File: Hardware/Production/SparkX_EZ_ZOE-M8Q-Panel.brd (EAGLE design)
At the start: 187.2 x 136.7 mm, 1506 parts, among them J1 U.FL, J10 U.FL, J11 U.FL, J12 U.FL, J13 U.FL, J14 U.FL, J15 U.FL, J16 U.FL, J17 U.FL, J18 U.FL, J19 U.FL, J2 U.FL, J20 U.FL, J21 U.FL, J22 U.FL, J23 U.FL, J24 U.FL, J25 U.FL, J26 U.FL, J27 U.FL, J28 U.FL, J29 U.FL, J3 U.FL, J30 U.FL, J4 U.FL, J5 U.FL, J6 U.FL, J7 U.FL, J8 U.FL, J9 U.FL, Q1 20V/4.2A/52mΩ/1.4W, Q10 20V/4.2A/52mΩ/1.4W, Q11 20V/4.2A/52mΩ/1.4W, Q12 20V/4.2A/52mΩ/1.4W, Q13 20V/4.2A/52mΩ/1.4W, Q14 20V/4.2A/52mΩ/1.4W, Q15 20V/4.2A/52mΩ/1.4W, Q16 20V/4.2A/52mΩ/1.4W, Q17 20V/4.2A/52mΩ/1.4W, Q18 20V/4.2A/52mΩ/1.4W, Q19 20V/4.2A/52mΩ/1.4W, Q2 20V/4.2A/52mΩ/1.4W, Q20 20V/4.2A/52mΩ/1.4W, Q21 20V/4.2A/52mΩ/1.4W, Q22 20V/4.2A/52mΩ/1.4W, Q23 20V/4.2A/52mΩ/1.4W, Q24 20V/4.2A/52mΩ/1.4W, Q25 20V/4.2A/52mΩ/1.4W, Q26 20V/4.2A/52mΩ/1.4W, Q27 20V/4.2A/52mΩ/1.4W, Q28 20V/4.2A/52mΩ/1.4W, Q29 20V/4.2A/52mΩ/1.4W, Q3 20V/4.2A/52mΩ/1.4W, Q30 20V/4.2A/52mΩ/1.4W, Q4 20V/4.2A/52mΩ/1.4W, Q5 20V/4.2A/52mΩ/1.4W, Q6 20V/4.2A/52mΩ/1.4W, Q7 20V/4.2A/52mΩ/1.4W, Q8 20V/4.2A/52mΩ/1.4W, Q9 20V/4.2A/52mΩ/1.4W, U1 U-BLOX_ZOE_M8Q-0-10, U10 U-BLOX_ZOE_M8Q-0-10, U11 U-BLOX_ZOE_M8Q-0-10, U12 U-BLOX_ZOE_M8Q-0-10, U13 U-BLOX_ZOE_M8Q-0-10, U14 U-BLOX_ZOE_M8Q-0-10, U15 U-BLOX_ZOE_M8Q-0-10, U16 U-BLOX_ZOE_M8Q-0-10, U17 U-BLOX_ZOE_M8Q-0-10, U18 U-BLOX_ZOE_M8Q-0-10, U19 U-BLOX_ZOE_M8Q-0-10, U2 U-BLOX_ZOE_M8Q-0-10, U20 U-BLOX_ZOE_M8Q-0-10, U21 U-BLOX_ZOE_M8Q-0-10, U22 U-BLOX_ZOE_M8Q-0-10, U23 U-BLOX_ZOE_M8Q-0-10, U24 U-BLOX_ZOE_M8Q-0-10, U25 U-BLOX_ZOE_M8Q-0-10, U26 U-BLOX_ZOE_M8Q-0-10, U27 U-BLOX_ZOE_M8Q-0-10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

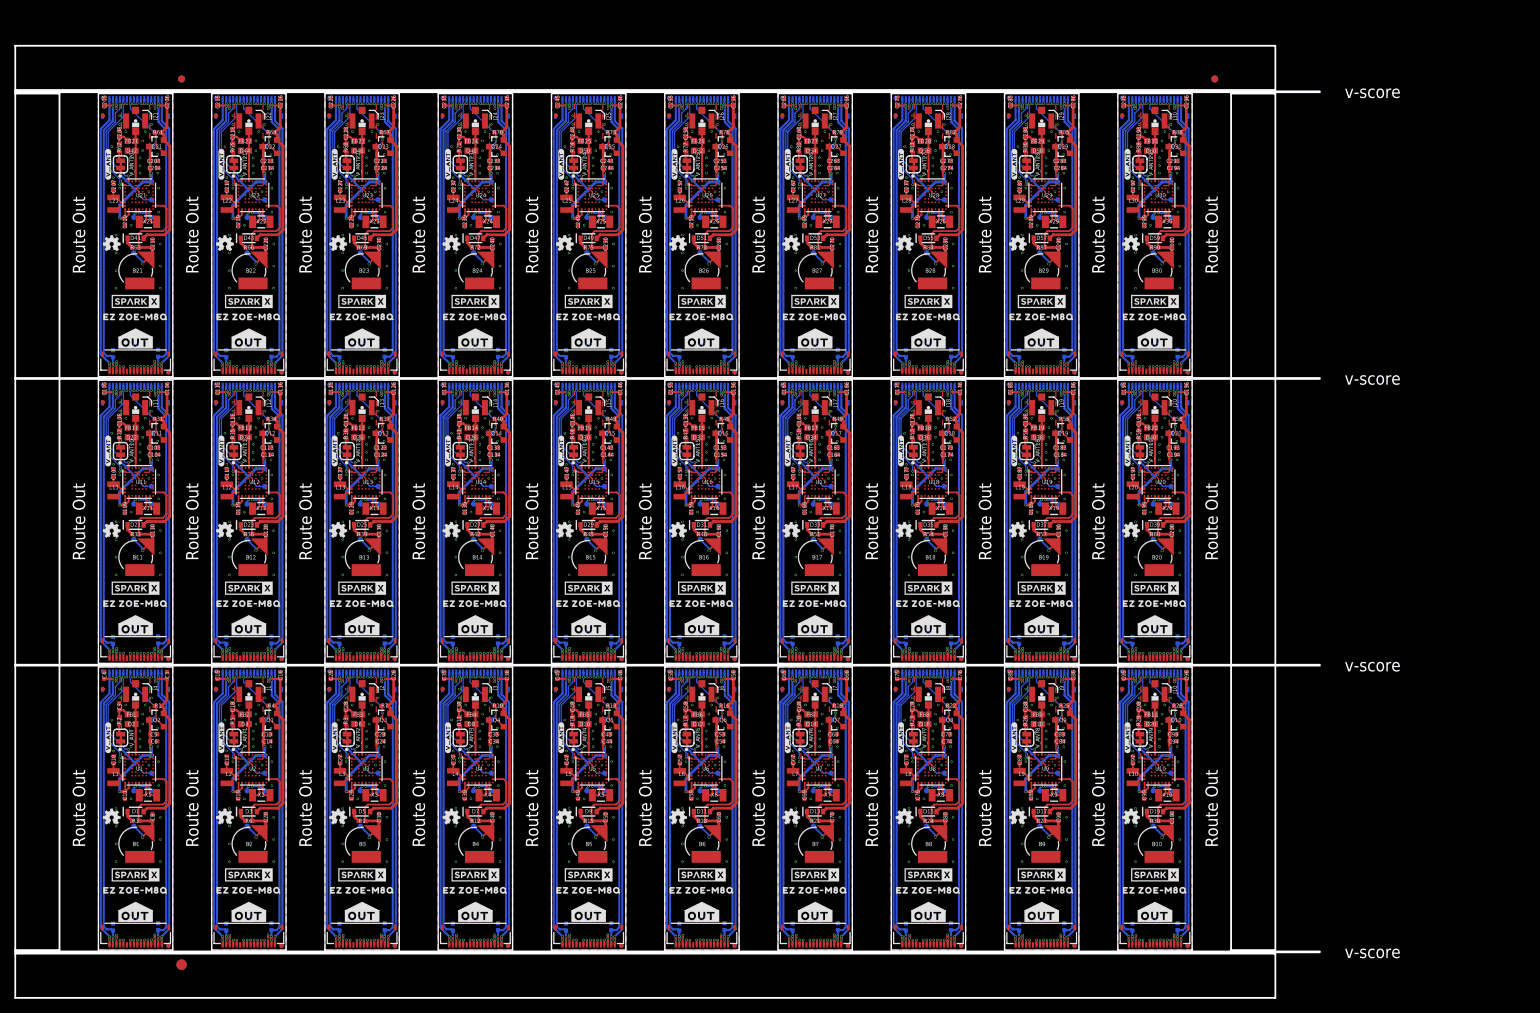
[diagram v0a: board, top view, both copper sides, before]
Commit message: Gapless production panel
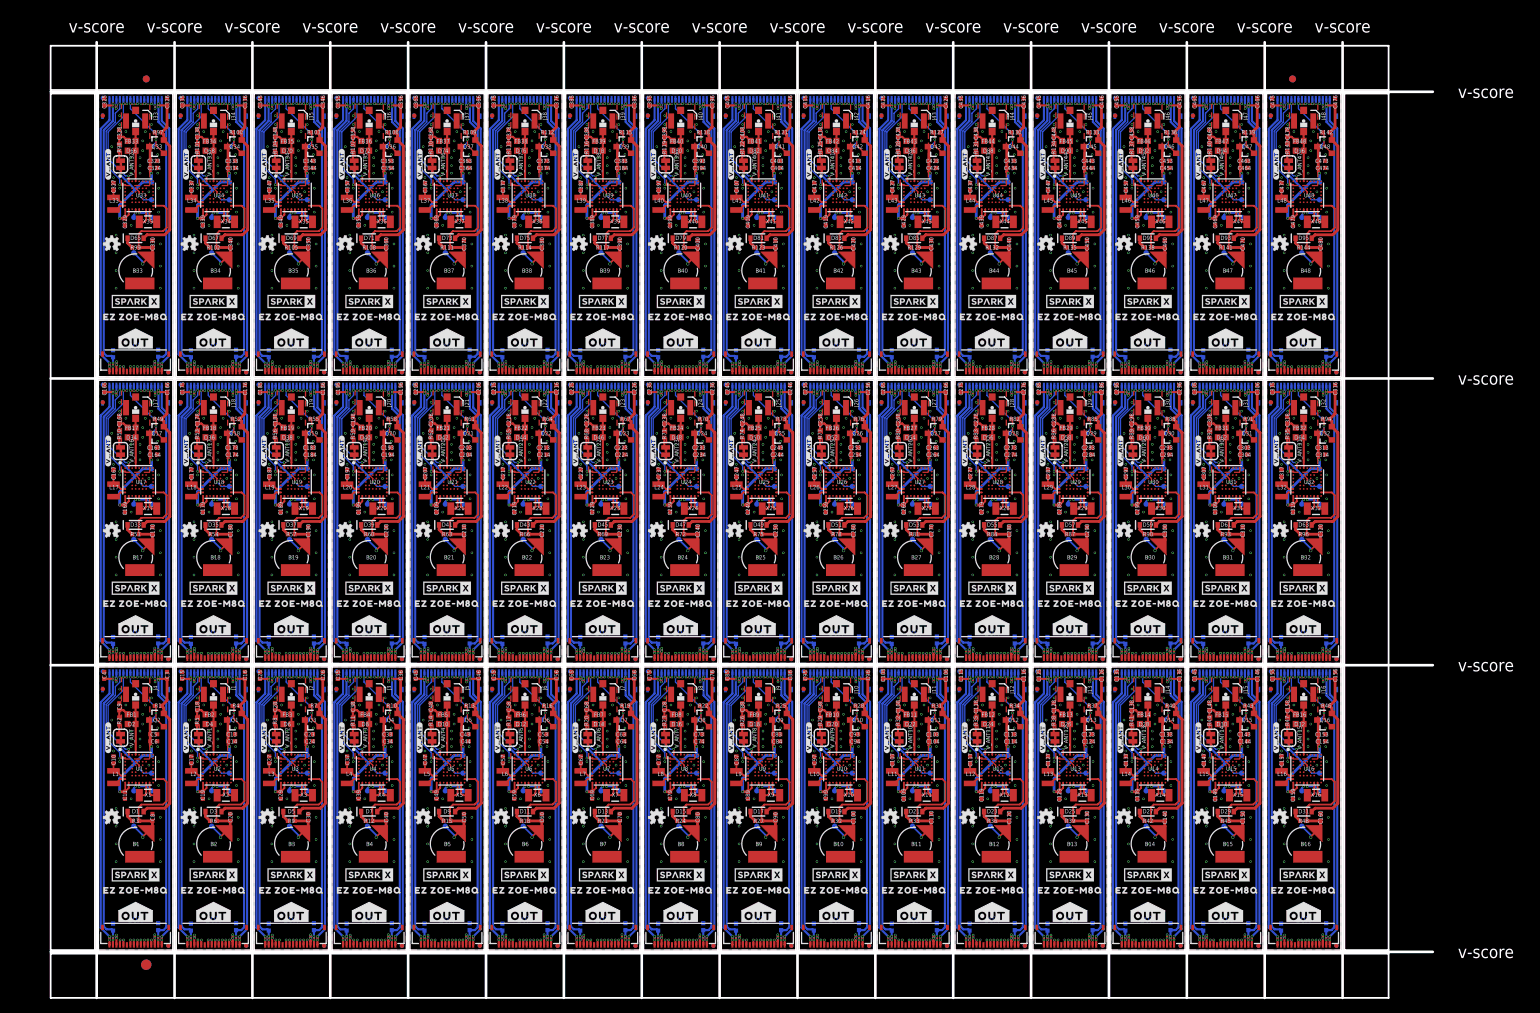
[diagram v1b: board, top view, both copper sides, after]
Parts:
- added !SAFEBOOT!30, !SAFEBOOT!31, !SAFEBOOT!32, !SAFEBOOT!33, !SAFEBOOT!34, !SAFEBOOT!35, !SAFEBOOT!36, !SAFEBOOT!37, !SAFEBOOT!38, !SAFEBOOT!39, !SAFEBOOT!40, !SAFEBOOT!41, !SAFEBOOT!42, !SAFEBOOT!43, !SAFEBOOT!44, !SAFEBOOT!45, !SAFEBOOT!46, !SAFEBOOT!47, GPIO30, GPIO31, GPIO32, GPIO33, GPIO34, GPIO35, GPIO36, GPIO37, GPIO38, GPIO39, GPIO40, GPIO41, GPIO42, GPIO43, GPIO44, GPIO45, GPIO46, GPIO47, RXD30, RXD31, RXD32, RXD33, RXD34, RXD35, RXD36, RXD37, RXD38, RXD39, RXD40, RXD41, RXD42, RXD43, RXD44, RXD45, RXD46, RXD47, TXD30, TXD31, TXD32, TXD33, TXD34, TXD35, TXD36, TXD37, TXD38, TXD39, TXD40, TXD41, TXD42, TXD43, TXD44, TXD45, TXD46, TXD47, VDD30, VDD31, VDD32, VDD33, VDD34, VDD35, VDD36, VDD37, VDD38, VDD39, VDD40, VDD41, VDD42, VDD43, VDD44, VDD45, VDD46, VDD47, V_BCKP30, V_BCKP31, V_BCKP32, V_BCKP33, V_BCKP34, V_BCKP35, V_BCKP36, V_BCKP37, V_BCKP38, V_BCKP39, V_BCKP40, V_BCKP41, V_BCKP42, V_BCKP43, V_BCKP44, V_BCKP45, V_BCKP46, V_BCKP47: TEST-POINT3, SparkFun-Connectors:PAD.03X.03
- added B31, B32, B33, B34, B35, B36, B37, B38, B39, B40, B41, B42, B43, B44, B45, B46, B47, B48: 6.8MM_COIN_CELL, SparkFun-Batteries:ML414H_IV01E
- added C301, C302, C303, C305, C306, C311, C312, C313, C315, C316, C321, C322, C323, C325, C326, C331, C332, C333, C335, C336, C341, C342, C343, C345, C346, C351, C352, C353, C355, C356, C361, C362, C363, C365, C366, C371, C372, C373, C375, C376, C381, C382, C383, C385, C386, C391, C392, C393, C395, C396, C401, C402, C403, C405, C406, C411, C412, C413, C415, C416, C421, C422, C423, C425, C426, C431, C432, C433, C435, C436, C441, C442, C443, C445, C446, C451, C452, C453, C455, C456, C461, C462, C463, C465, C466, C471, C472, C473, C475, C476: 2.2uF, SparkFun-Capacitors:0402-TIGHT
- added C304, C309, C314, C319, C324, C329, C334, C339, C344, C349, C354, C359, C364, C369, C374, C379, C384, C389, C394, C399, C404, C409, C414, C419, C424, C429, C434, C439, C444, C449, C454, C459, C464, C469, C474, C479: 0.1uF, SparkFun-Capacitors:0402-TIGHT
- added C307, C317, C327, C337, C347, C357, C367, C377, C387, C397, C407, C417, C427, C437, C447, C457, C467, C477: 4.7uF, SparkFun-Capacitors:0402-TIGHT
- added C308, C318, C328, C338, C348, C358, C368, C378, C388, C398, C408, C418, C428, C438, C448, C458, C468, C478: 47PF-0402_TIGHT-25V-5%-X7R, SparkFun-Capacitors:0402-TIGHT
- added C310, C320, C330, C340, C350, C360, C370, C380, C390, C400, C410, C420, C430, C440, C450, C460, C470, C480: 1.0uF, SparkFun-Capacitors:0402-TIGHT
- added D61, D63, D65, D67, D69, D71, D73, D75, D77, D79, D81, D83, D85, D87, D89, D91, D93, D95: 1A/23V/620mV, SparkFun-DiscreteSemi:SOD-323
- added D62, D64, D66, D68, D70, D72, D74, D76, D78, D80, D82, D84, D86, D88, D90, D92, D94, D96: PESD0402, SparkFun-DiscreteSemi:0402
- added FB31, FB32, FB33, FB34, FB35, FB36, FB37, FB38, FB39, FB40, FB41, FB42, FB43, FB44, FB45, FB46, FB47, FB48: FERRITE_BEAD-120_OHM-0402, SparkFun-Coils:0402
- added FD121, FD122, FD123, FD124, FD125, FD126, FD127, FD128, FD129, FD130, FD131, FD132, FD133, FD134, FD135, FD136, FD137, FD138, FD139, FD140, FD141, FD142, FD143, FD144, FD145, FD146, FD147, FD148, FD149, FD150, FD151, FD152, FD153, FD154, FD155, FD156, FD157, FD158, FD159, FD160, FD161, FD162, FD163, FD164, FD165, FD166, FD167, FD168, FD169, FD170, FD171, FD172, FD173, FD174, FD175, FD176, FD177, FD178, FD179, FD180, FD181, FD182, FD183, FD184, FD185, FD186, FD187, FD188, FD189, FD190, FD191, FD192: FIDUCIALUFIDUCIAL, SparkFun-Aesthetics:FIDUCIAL-MICRO
- added IN30, IN31, IN32, IN33, IN34, IN35, IN36, IN37, IN38, IN39, IN40, IN41, IN42, IN43, IN44, IN45, IN46, IN47, OUT30, OUT31, OUT32, OUT33, OUT34, OUT35, OUT36, OUT37, OUT38, OUT39, OUT40, OUT41, OUT42, OUT43, OUT44, OUT45, OUT46, OUT47: FPC_16_0.5MM_BACKFLIP, New_Parts_Connectors:FPC_16_DOUBLESIDED_BACKFLIP
- added J31, J32, J33, J34, J35, J36, J37, J38, J39, J40, J41, J42, J43, J44, J45, J46, J47, J48: U.FL, SparkFun-Connectors:U.FL
- added L31, L32, L33, L34, L35, L36, L37, L38, L39, L40, L41, L42, L43, L44, L45, L46, L47, L48: 2.2uH, SparkFun-Coils:0806
- added LOGO61, LOGO62, LOGO63, LOGO64, LOGO65, LOGO66, LOGO67, LOGO68, LOGO69, LOGO70, LOGO71, LOGO72, LOGO73, LOGO74, LOGO75, LOGO76, LOGO77, LOGO78, LOGO79, LOGO80, LOGO81, LOGO82, LOGO83, LOGO84, LOGO85, LOGO86, LOGO87, LOGO88, LOGO89, LOGO90, LOGO91, LOGO92, LOGO93, LOGO94, LOGO95, LOGO96: OSHW-LOGOMINI, SparkFun-Aesthetics:OSHW-LOGO-MINI
- added Q31, Q32, Q33, Q34, Q35, Q36, Q37, Q38, Q39, Q40, Q41, Q42, Q43, Q44, Q45, Q46, Q47, Q48: 20V/4.2A/52mΩ/1.4W, SparkFun-DiscreteSemi:SOT23-3
- added R100, R103, R106, R109, R112, R115, R118, R121, R124, R127, R130, R133, R136, R139, R142, R91, R94, R97: 100k, SparkFun-Resistors:0402-TIGHT
- added R101, R104, R107, R110, R113, R116, R119, R122, R125, R128, R131, R134, R137, R140, R143, R92, R95, R98: 2, SparkFun-Resistors:0402-TIGHT
- added R102, R105, R108, R111, R114, R117, R120, R123, R126, R129, R132, R135, R138, R141, R144, R93, R96, R99: 1k, SparkFun-Resistors:0402-TIGHT
- added U$391, U$392, U$404, U$405, U$417, U$418, U$430, U$431, U$443, U$444, U$456, U$457, U$469, U$470, U$482, U$483, U$495, U$496, U$508, U$509, U$521, U$522, U$534, U$535, U$547, U$548, U$560, U$561, U$573, U$574, U$586, U$587, U$599, U$600, U$612, U$613: SPARKX-LOGO3, SparkX:SPARKX-SMALL
- added U$393, U$394, U$406, U$407, U$419, U$420, U$432, U$433, U$445, U$446, U$458, U$459, U$471, U$472, U$484, U$485, U$497, U$498, U$510, U$511, U$523, U$524, U$536, U$537, U$549, U$550, U$562, U$563, U$575, U$576, U$588, U$589, U$601, U$602, U$614, U$615: (no value), output:EZ_ZOE#M8Q0
- added U$395, U$408, U$421, U$434, U$447, U$460, U$473, U$486, U$499, U$512, U$525, U$538, U$551, U$564, U$577, U$590, U$603, U$616: (no value), output:#V_ANT#0
- added U$396, U$409, U$422, U$435, U$448, U$461, U$474, U$487, U$500, U$513, U$526, U$539, U$552, U$565, U$578, U$591, U$604, U$617: (no value), output:#VDD#0
- added U$397, U$410, U$423, U$436, U$449, U$462, U$475, U$488, U$501, U$514, U$527, U$540, U$553, U$566, U$579, U$592, U$605, U$618: (no value), output:##SAFEBOOT##0
- added U$398, U$411, U$424, U$437, U$450, U$463, U$476, U$489, U$502, U$515, U$528, U$541, U$554, U$567, U$580, U$593, U$606, U$619: (no value), output:#TXD#0
- added U$399, U$412, U$425, U$438, U$451, U$464, U$477, U$490, U$503, U$516, U$529, U$542, U$555, U$568, U$581, U$594, U$607, U$620: (no value), output:#RXD#0
- added U$400, U$413, U$426, U$439, U$452, U$465, U$478, U$491, U$504, U$517, U$530, U$543, U$556, U$569, U$582, U$595, U$608, U$621: (no value), output:#GPIO0#0
- added U$401, U$414, U$427, U$440, U$453, U$466, U$479, U$492, U$505, U$518, U$531, U$544, U$557, U$570, U$583, U$596, U$609, U$622: (no value), output:#V_BCKP#0
- added U$402, U$415, U$428, U$441, U$454, U$467, U$480, U$493, U$506, U$519, U$532, U$545, U$558, U$571, U$584, U$597, U$610, U$623: (no value), output:#IN#0
- added U$403, U$416, U$429, U$442, U$455, U$468, U$481, U$494, U$507, U$520, U$533, U$546, U$559, U$572, U$585, U$598, U$611, U$624: (no value), output:#OUT#0
- added U31, U32, U33, U34, U35, U36, U37, U38, U39, U40, U41, U42, U43, U44, U45, U46, U47, U48: U-BLOX_ZOE_M8Q-0-10, SparkFun-GPS:UBLOX_ZOE_M8-0-10
- added V_ANT30, V_ANT31, V_ANT32, V_ANT33, V_ANT34, V_ANT35, V_ANT36, V_ANT37, V_ANT38, V_ANT39, V_ANT40, V_ANT41, V_ANT42, V_ANT43, V_ANT44, V_ANT45, V_ANT46, V_ANT47: JUMPER-SMT_2_NC_TRACE_SILK, SparkFun-Jumpers:SMT-JUMPER_2_NC_TRACE_SILK
- added X31, X32, X33, X34, X35, X36, X37, X38, X39, X40, X41, X42, X43, X44, X45, X46, X47, X48: 32.768kHz, SparkFun-Clocks:CRYSTAL-SMD-3.2X1.5MM
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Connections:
- new net !SAFEBOOT!30: !SAFEBOOT!30.1, U31.34
- new net !SAFEBOOT!31: !SAFEBOOT!31.1, U32.34
- new net !SAFEBOOT!32: !SAFEBOOT!32.1, U33.34
- new net !SAFEBOOT!33: !SAFEBOOT!33.1, U34.34
- new net !SAFEBOOT!34: !SAFEBOOT!34.1, U35.34
- new net !SAFEBOOT!35: !SAFEBOOT!35.1, U36.34
- new net !SAFEBOOT!36: !SAFEBOOT!36.1, U37.34
- new net !SAFEBOOT!37: !SAFEBOOT!37.1, U38.34
- new net !SAFEBOOT!38: !SAFEBOOT!38.1, U39.34
- new net !SAFEBOOT!39: !SAFEBOOT!39.1, U40.34
- new net !SAFEBOOT!40: !SAFEBOOT!40.1, U41.34
- new net !SAFEBOOT!41: !SAFEBOOT!41.1, U42.34
- new net !SAFEBOOT!42: !SAFEBOOT!42.1, U43.34
- new net !SAFEBOOT!43: !SAFEBOOT!43.1, U44.34
- new net !SAFEBOOT!44: !SAFEBOOT!44.1, U45.34
- new net !SAFEBOOT!45: !SAFEBOOT!45.1, U46.34
- new net !SAFEBOOT!46: !SAFEBOOT!46.1, U47.34
- new net !SAFEBOOT!47: !SAFEBOOT!47.1, U48.34
- new net 3.3V30: C301.1, C302.1, C305.1, C306.1, D61.A, IN30.15, IN30.2, OUT30.15, OUT30.2, Q31.2, R91.2
- new net 3.3V31: C311.1, C312.1, C315.1, C316.1, D63.A, IN31.15, IN31.2, OUT31.15, OUT31.2, Q32.2, R94.2
- new net 3.3V32: C321.1, C322.1, C325.1, C326.1, D65.A, IN32.15, IN32.2, OUT32.15, OUT32.2, Q33.2, R97.2
- new net 3.3V33: C331.1, C332.1, C335.1, C336.1, D67.A, IN33.15, IN33.2, OUT33.15, OUT33.2, Q34.2, R100.2
- new net 3.3V34: C341.1, C342.1, C345.1, C346.1, D69.A, IN34.15, IN34.2, OUT34.15, OUT34.2, Q35.2, R103.2
- new net 3.3V35: C351.1, C352.1, C355.1, C356.1, D71.A, IN35.15, IN35.2, OUT35.15, OUT35.2, Q36.2, R106.2
- new net 3.3V36: C361.1, C362.1, C365.1, C366.1, D73.A, IN36.15, IN36.2, OUT36.15, OUT36.2, Q37.2, R109.2
- new net 3.3V37: C371.1, C372.1, C375.1, C376.1, D75.A, IN37.15, IN37.2, OUT37.15, OUT37.2, Q38.2, R112.2
- new net 3.3V38: C381.1, C382.1, C385.1, C386.1, D77.A, IN38.15, IN38.2, OUT38.15, OUT38.2, Q39.2, R115.2
- new net 3.3V39: C391.1, C392.1, C395.1, C396.1, D79.A, IN39.15, IN39.2, OUT39.15, OUT39.2, Q40.2, R118.2
- new net 3.3V40: C401.1, C402.1, C405.1, C406.1, D81.A, IN40.15, IN40.2, OUT40.15, OUT40.2, Q41.2, R121.2
- new net 3.3V41: C411.1, C412.1, C415.1, C416.1, D83.A, IN41.15, IN41.2, OUT41.15, OUT41.2, Q42.2, R124.2
- new net 3.3V42: C421.1, C422.1, C425.1, C426.1, D85.A, IN42.15, IN42.2, OUT42.15, OUT42.2, Q43.2, R127.2
- new net 3.3V43: C431.1, C432.1, C435.1, C436.1, D87.A, IN43.15, IN43.2, OUT43.15, OUT43.2, Q44.2, R130.2
- new net 3.3V44: C441.1, C442.1, C445.1, C446.1, D89.A, IN44.15, IN44.2, OUT44.15, OUT44.2, Q45.2, R133.2
- new net 3.3V45: C451.1, C452.1, C455.1, C456.1, D91.A, IN45.15, IN45.2, OUT45.15, OUT45.2, Q46.2, R136.2
- new net 3.3V46: C461.1, C462.1, C465.1, C466.1, D93.A, IN46.15, IN46.2, OUT46.15, OUT46.2, Q47.2, R139.2
- new net 3.3V47: C471.1, C472.1, C475.1, C476.1, D95.A, IN47.15, IN47.2, OUT47.15, OUT47.2, Q48.2, R142.2
- new net ANT30: D62.2, FB31.1, J31.FEED, U31.4
- new net ANT31: D64.2, FB32.1, J32.FEED, U32.4
- new net ANT32: D66.2, FB33.1, J33.FEED, U33.4
- new net ANT33: D68.2, FB34.1, J34.FEED, U34.4
- new net ANT34: D70.2, FB35.1, J35.FEED, U35.4
- new net ANT35: D72.2, FB36.1, J36.FEED, U36.4
- new net ANT36: D74.2, FB37.1, J37.FEED, U37.4
- new net ANT37: D76.2, FB38.1, J38.FEED, U38.4
- new net ANT38: D78.2, FB39.1, J39.FEED, U39.4
- new net ANT39: D80.2, FB40.1, J40.FEED, U40.4
- new net ANT40: D82.2, FB41.1, J41.FEED, U41.4
- new net ANT41: D84.2, FB42.1, J42.FEED, U42.4
- new net ANT42: D86.2, FB43.1, J43.FEED, U43.4
- new net ANT43: D88.2, FB44.1, J44.FEED, U44.4
- new net ANT44: D90.2, FB45.1, J45.FEED, U45.4
- new net ANT45: D92.2, FB46.1, J46.FEED, U46.4
- new net ANT46: D94.2, FB47.1, J47.FEED, U47.4
- new net ANT47: D96.2, FB48.1, J48.FEED, U48.4
- new net CIPO30: IN30.6, OUT30.6
- new net CIPO31: IN31.6, OUT31.6
- new net CIPO32: IN32.6, OUT32.6
- new net CIPO33: IN33.6, OUT33.6
- new net CIPO34: IN34.6, OUT34.6
- new net CIPO35: IN35.6, OUT35.6
- new net CIPO36: IN36.6, OUT36.6
- new net CIPO37: IN37.6, OUT37.6
- new net CIPO38: IN38.6, OUT38.6
- new net CIPO39: IN39.6, OUT39.6
- new net CIPO40: IN40.6, OUT40.6
- new net CIPO41: IN41.6, OUT41.6
- new net CIPO42: IN42.6, OUT42.6
- new net CIPO43: IN43.6, OUT43.6
- new net CIPO44: IN44.6, OUT44.6
- new net CIPO45: IN45.6, OUT45.6
- new net CIPO46: IN46.6, OUT46.6
- new net CIPO47: IN47.6, OUT47.6
- new net COPI30: IN30.5, OUT30.5
- new net COPI31: IN31.5, OUT31.5
- new net COPI32: IN32.5, OUT32.5
- new net COPI33: IN33.5, OUT33.5
- new net COPI34: IN34.5, OUT34.5
- new net COPI35: IN35.5, OUT35.5
- new net COPI36: IN36.5, OUT36.5
- new net COPI37: IN37.5, OUT37.5
- new net COPI38: IN38.5, OUT38.5
- new net COPI39: IN39.5, OUT39.5
- new net COPI40: IN40.5, OUT40.5
- new net COPI41: IN41.5, OUT41.5
- new net COPI42: IN42.5, OUT42.5
- new net COPI43: IN43.5, OUT43.5
- new net COPI44: IN44.5, OUT44.5
- new net COPI45: IN45.5, OUT45.5
- new net COPI46: IN46.5, OUT46.5
- new net COPI47: IN47.5, OUT47.5
- new net CS100: IN33.8, OUT33.8
- new net CS101: IN33.9, OUT33.9
- new net CS102: IN34.7, OUT34.7
- new net CS103: IN34.8, OUT34.8
- new net CS104: IN34.9, OUT34.9
- new net CS105: IN35.7, OUT35.7
- new net CS106: IN35.8, OUT35.8
- new net CS107: IN35.9, OUT35.9
- new net CS108: IN36.7, OUT36.7
- new net CS109: IN36.8, OUT36.8
- new net CS110: IN36.9, OUT36.9
- new net CS111: IN37.7, OUT37.7
- new net CS112: IN37.8, OUT37.8
- new net CS113: IN37.9, OUT37.9
- new net CS114: IN38.7, OUT38.7
- new net CS115: IN38.8, OUT38.8
- new net CS116: IN38.9, OUT38.9
- new net CS117: IN39.7, OUT39.7
- new net CS118: IN39.8, OUT39.8
- new net CS119: IN39.9, OUT39.9
- new net CS120: IN40.7, OUT40.7
- new net CS121: IN40.8, OUT40.8
- new net CS122: IN40.9, OUT40.9
- new net CS123: IN41.7, OUT41.7
- new net CS124: IN41.8, OUT41.8
- new net CS125: IN41.9, OUT41.9
- new net CS126: IN42.7, OUT42.7
- new net CS127: IN42.8, OUT42.8
- new net CS128: IN42.9, OUT42.9
- new net CS129: IN43.7, OUT43.7
- new net CS130: IN43.8, OUT43.8
- new net CS131: IN43.9, OUT43.9
- new net CS132: IN44.7, OUT44.7
- new net CS133: IN44.8, OUT44.8
- new net CS134: IN44.9, OUT44.9
- new net CS135: IN45.7, OUT45.7
- new net CS136: IN45.8, OUT45.8
- new net CS137: IN45.9, OUT45.9
- new net CS138: IN46.7, OUT46.7
- new net CS139: IN46.8, OUT46.8
- new net CS140: IN46.9, OUT46.9
- new net CS141: IN47.7, OUT47.7
- new net CS142: IN47.8, OUT47.8
- new net CS143: IN47.9, OUT47.9
- new net CS90: IN30.7, OUT30.7
- new net CS91: IN30.8, OUT30.8
- new net CS92: IN30.9, OUT30.9
- new net CS93: IN31.7, OUT31.7
- new net CS94: IN31.8, OUT31.8
- new net CS95: IN31.9, OUT31.9
- new net CS96: IN32.7, OUT32.7
- new net CS97: IN32.8, OUT32.8
- new net CS98: IN32.9, OUT32.9
- new net CS99: IN33.7, OUT33.7
- new net GND30: B31.-, C301.2, C302.2, C303.2, C304.2, C305.2, C306.2, C307.2, C308.2, C309.2, C310.2, D62.1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
- new net GND31: B32.-, C311.2, C312.2, C313.2, C314.2, C315.2, C316.2, C317.2, C318.2, C319.2, C320.2, D64.1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
- new net GND32: B33.-, C321.2, C322.2, C323.2, C324.2, C325.2, C326.2, C327.2, C328.2, C329.2, C330.2, D66.1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
- new net GND33: B34.-, C331.2, C332.2, C333.2, C334.2, C335.2, C336.2, C337.2, C338.2, C339.2, C340.2, D68.1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
- new net GND34: B35.-, C341.2, C342.2, C343.2, C344.2, C345.2, C346.2, C347.2, C348.2, C349.2, C350.2, D70.1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
- new net GND35: B36.-, C351.2, C352.2, C353.2, C354.2, C355.2, C356.2, C357.2, C358.2, C359.2, C360.2, D72.1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
- new net GND36: B37.-, C361.2, C362.2, C363.2, C364.2, C365.2, C366.2, C367.2, C368.2, C369.2, C370.2, D74.1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
- new net GND37: B38.-, C371.2, C372.2, C373.2, C374.2, C375.2, C376.2, C377.2, C378.2, C379.2, C380.2, D76.1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
- new net GND38: B39.-, C381.2, C382.2, C383.2, C384.2, C385.2, C386.2, C387.2, C388.2, C389.2, C390.2, D78.1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
- new net GND39: B40.-, C391.2, C392.2, C393.2, C394.2, C395.2, C396.2, C397.2, C398.2, C399.2, C400.2, D80.1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
- new net GND40: B41.-, C401.2, C402.2, C403.2, C404.2, C405.2, C406.2, C407.2, C408.2, C409.2, C410.2, D82.1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
- new net GND41: B42.-, C411.2, C412.2, C413.2, C414.2, C415.2, C416.2, C417.2, C418.2, C419.2, C420.2, D84.1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
- new net GND42: B43.-, C421.2, C422.2, C423.2, C424.2, C425.2, C426.2, C427.2, C428.2, C429.2, C430.2, D86.1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
- new net GND43: B44.-, C431.2, C432.2, C433.2, C434.2, C435.2, C436.2, C437.2, C438.2, C439.2, C440.2, D88.1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
- new net GND44: B45.-, C441.2, C442.2, C443.2, C444.2, C445.2, C446.2, C447.2, C448.2, C449.2, C450.2, D90.1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
- new net GND45: B46.-, C451.2, C452.2, C453.2, C454.2, C455.2, C456.2, C457.2, C458.2, C459.2, C460.2, D92.1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
- new net GND46: B47.-, C461.2, C462.2, C463.2, C464.2, C465.2, C466.2, C467.2, C468.2, C469.2, C470.2, D94.1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
- new net GND47: B48.-, C471.2, C472.2, C473.2, C474.2, C475.2, C476.2, C477.2, C478.2, C479.2, C480.2, D96.1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
- new net GPIO60: GPIO30.1, IN30.10, Q31.1, R91.1
- new net GPIO61: IN30.11, OUT30.10
- new net GPIO62: GPIO31.1, IN31.10, Q32.1, R94.1
- new net GPIO63: IN31.11, OUT31.10
- new net GPIO64: GPIO32.1, IN32.10, Q33.1, R97.1
- new net GPIO65: IN32.11, OUT32.10
- new net GPIO66: GPIO33.1, IN33.10, Q34.1, R100.1
- new net GPIO67: IN33.11, OUT33.10
- new net GPIO68: GPIO34.1, IN34.10, Q35.1, R103.1
- new net GPIO69: IN34.11, OUT34.10
- new net GPIO70: GPIO35.1, IN35.10, Q36.1, R106.1
- new net GPIO71: IN35.11, OUT35.10
- new net GPIO72: GPIO36.1, IN36.10, Q37.1, R109.1
- new net GPIO73: IN36.11, OUT36.10
- new net GPIO74: GPIO37.1, IN37.10, Q38.1, R112.1
- new net GPIO75: IN37.11, OUT37.10
- new net GPIO76: GPIO38.1, IN38.10, Q39.1, R115.1
- new net GPIO77: IN38.11, OUT38.10
- new net GPIO78: GPIO39.1, IN39.10, Q40.1, R118.1
- new net GPIO79: IN39.11, OUT39.10
- new net GPIO80: GPIO40.1, IN40.10, Q41.1, R121.1
- new net GPIO81: IN40.11, OUT40.10
- new net GPIO82: GPIO41.1, IN41.10, Q42.1, R124.1
- new net GPIO83: IN41.11, OUT41.10
- new net GPIO84: GPIO42.1, IN42.10, Q43.1, R127.1
- new net GPIO85: IN42.11, OUT42.10
- new net GPIO86: GPIO43.1, IN43.10, Q44.1, R130.1
- new net GPIO87: IN43.11, OUT43.10
- new net GPIO88: GPIO44.1, IN44.10, Q45.1, R133.1
- new net GPIO89: IN44.11, OUT44.10
- new net GPIO90: GPIO45.1, IN45.10, Q46.1, R136.1
- new net GPIO91: IN45.11, OUT45.10
- new net GPIO92: GPIO46.1, IN46.10, Q47.1, R139.1
- new net GPIO93: IN46.11, OUT46.10
- new net GPIO94: GPIO47.1, IN47.10, Q48.1, R142.1
- new net GPIO95: IN47.11, OUT47.10
- new net N$211: L31.2, U31.26
- new net N$212: C307.1, L31.1, U31.27
- new net N$213: U31.18, X31.P$2
- new net N$214: U31.19, X31.P$1
- new net N$215: C308.1, FB31.2, R92.1
- new net N$216: R92.2, V_ANT30.1
- new net N$217: D61.C, R93.2
- new net N$218: L32.2, U32.26
- new net N$219: C317.1, L32.1, U32.27
- new net N$220: U32.18, X32.P$2
- new net N$221: U32.19, X32.P$1
- new net N$222: C318.1, FB32.2, R95.1
- new net N$223: R95.2, V_ANT31.1
- new net N$224: D63.C, R96.2
- new net N$225: L33.2, U33.26
- new net N$226: C327.1, L33.1, U33.27
- new net N$227: U33.18, X33.P$2
- new net N$228: U33.19, X33.P$1
- new net N$229: C328.1, FB33.2, R98.1
- new net N$230: R98.2, V_ANT32.1
- new net N$231: D65.C, R99.2
- new net N$232: L34.2, U34.26
- new net N$233: C337.1, L34.1, U34.27
- new net N$234: U34.18, X34.P$2
- new net N$235: U34.19, X34.P$1
- new net N$236: C338.1, FB34.2, R101.1
- new net N$237: R101.2, V_ANT33.1
- new net N$238: D67.C, R102.2
- new net N$239: L35.2, U35.26
- new net N$240: C347.1, L35.1, U35.27
- new net N$241: U35.18, X35.P$2
- new net N$242: U35.19, X35.P$1
- new net N$243: C348.1, FB35.2, R104.1
- new net N$244: R104.2, V_ANT34.1
- new net N$245: D69.C, R105.2
- new net N$246: L36.2, U36.26
- new net N$247: C357.1, L36.1, U36.27
- new net N$248: U36.18, X36.P$2
- new net N$249: U36.19, X36.P$1
- new net N$250: C358.1, FB36.2, R107.1
- new net N$251: R107.2, V_ANT35.1
- new net N$252: D71.C, R108.2
- new net N$253: L37.2, U37.26
- new net N$254: C367.1, L37.1, U37.27
- new net N$255: U37.18, X37.P$2
- new net N$256: U37.19, X37.P$1
- new net N$257: C368.1, FB37.2, R110.1
- new net N$258: R110.2, V_ANT36.1
- new net N$259: D73.C, R111.2
- new net N$260: L38.2, U38.26
- new net N$261: C377.1, L38.1, U38.27
- new net N$262: U38.18, X38.P$2
- new net N$263: U38.19, X38.P$1
- new net N$264: C378.1, FB38.2, R113.1
- new net N$265: R113.2, V_ANT37.1
- new net N$266: D75.C, R114.2
- new net N$267: L39.2, U39.26
- new net N$268: C387.1, L39.1, U39.27
- new net N$269: U39.18, X39.P$2
- new net N$270: U39.19, X39.P$1
- new net N$271: C388.1, FB39.2, R116.1
- new net N$272: R116.2, V_ANT38.1
- new net N$273: D77.C, R117.2
- new net N$274: L40.2, U40.26
- new net N$275: C397.1, L40.1, U40.27
- new net N$276: U40.18, X40.P$2
- new net N$277: U40.19, X40.P$1
- new net N$278: C398.1, FB40.2, R119.1
- new net N$279: R119.2, V_ANT39.1
- new net N$280: D79.C, R120.2
- new net N$281: L41.2, U41.26
- new net N$282: C407.1, L41.1, U41.27
- new net N$283: U41.18, X41.P$2
- new net N$284: U41.19, X41.P$1
- new net N$285: C408.1, FB41.2, R122.1
- new net N$286: R122.2, V_ANT40.1
- new net N$287: D81.C, R123.2
- new net N$288: L42.2, U42.26
- new net N$289: C417.1, L42.1, U42.27
- new net N$290: U42.18, X42.P$2
- new net N$291: U42.19, X42.P$1
- new net N$292: C418.1, FB42.2, R125.1
- new net N$293: R125.2, V_ANT41.1
- new net N$294: D83.C, R126.2
- new net N$295: L43.2, U43.26
- new net N$296: C427.1, L43.1, U43.27
- new net N$297: U43.18, X43.P$2
- new net N$298: U43.19, X43.P$1
- new net N$299: C428.1, FB43.2, R128.1
- new net N$300: R128.2, V_ANT42.1
- new net N$301: D85.C, R129.2
- new net N$302: L44.2, U44.26
- new net N$303: C437.1, L44.1, U44.27
- new net N$304: U44.18, X44.P$2
- new net N$305: U44.19, X44.P$1
- new net N$306: C438.1, FB44.2, R131.1
- new net N$307: R131.2, V_ANT43.1
- new net N$308: D87.C, R132.2
- new net N$309: L45.2, U45.26
- new net N$310: C447.1, L45.1, U45.27
- new net N$311: U45.18, X45.P$2
- new net N$312: U45.19, X45.P$1
- new net N$313: C448.1, FB45.2, R134.1
- new net N$314: R134.2, V_ANT44.1
- new net N$315: D89.C, R135.2
- new net N$316: L46.2, U46.26
- new net N$317: C457.1, L46.1, U46.27
- new net N$318: U46.18, X46.P$2
- new net N$319: U46.19, X46.P$1
- new net N$320: C458.1, FB46.2, R137.1
- new net N$321: R137.2, V_ANT45.1
- new net N$322: D91.C, R138.2
- new net N$323: L47.2, U47.26
- new net N$324: C467.1, L47.1, U47.27
- new net N$325: U47.18, X47.P$2
- new net N$326: U47.19, X47.P$1
- new net N$327: C468.1, FB47.2, R140.1
- new net N$328: R140.2, V_ANT46.1
- new net N$329: D93.C, R141.2
- new net N$330: L48.2, U48.26
- new net N$331: C477.1, L48.1, U48.27
- new net N$332: U48.18, X48.P$2
- new net N$333: U48.19, X48.P$1
- new net N$334: C478.1, FB48.2, R143.1
- new net N$335: R143.2, V_ANT47.1
- new net N$336: D95.C, R144.2
- new net PROC_PWR_EN30: IN30.1, OUT30.1
- new net PROC_PWR_EN31: IN31.1, OUT31.1
- new net PROC_PWR_EN32: IN32.1, OUT32.1
- new net PROC_PWR_EN33: IN33.1, OUT33.1
- new net PROC_PWR_EN34: IN34.1, OUT34.1
- new net PROC_PWR_EN35: IN35.1, OUT35.1
- new net PROC_PWR_EN36: IN36.1, OUT36.1
- new net PROC_PWR_EN37: IN37.1, OUT37.1
- new net PROC_PWR_EN38: IN38.1, OUT38.1
- new net PROC_PWR_EN39: IN39.1, OUT39.1
- new net PROC_PWR_EN40: IN40.1, OUT40.1
- new net PROC_PWR_EN41: IN41.1, OUT41.1
- new net PROC_PWR_EN42: IN42.1, OUT42.1
- new net PROC_PWR_EN43: IN43.1, OUT43.1
- new net PROC_PWR_EN44: IN44.1, OUT44.1
- new net PROC_PWR_EN45: IN45.1, OUT45.1
- new net PROC_PWR_EN46: IN46.1, OUT46.1
- new net PROC_PWR_EN47: IN47.1, OUT47.1
- new net RXD30: RXD30.1, U31.22
- new net RXD31: RXD31.1, U32.22
- new net RXD32: RXD32.1, U33.22
- new net RXD33: RXD33.1, U34.22
- new net RXD34: RXD34.1, U35.22
- new net RXD35: RXD35.1, U36.22
- new net RXD36: RXD36.1, U37.22
- new net RXD37: RXD37.1, U38.22
- new net RXD38: RXD38.1, U39.22
- new net RXD39: RXD39.1, U40.22
- new net RXD40: RXD40.1, U41.22
- new net RXD41: RXD41.1, U42.22
- new net RXD42: RXD42.1, U43.22
- new net RXD43: RXD43.1, U44.22
- new net RXD44: RXD44.1, U45.22
- new net RXD45: RXD45.1, U46.22
- new net RXD46: RXD46.1, U47.22
- new net RXD47: RXD47.1, U48.22
- new net SCL30: IN30.13, OUT30.13, U31.32
- new net SCL31: IN31.13, OUT31.13, U32.32
- new net SCL32: IN32.13, OUT32.13, U33.32
- new net SCL33: IN33.13, OUT33.13, U34.32
- new net SCL34: IN34.13, OUT34.13, U35.32
- new net SCL35: IN35.13, OUT35.13, U36.32
- new net SCL36: IN36.13, OUT36.13, U37.32
- new net SCL37: IN37.13, OUT37.13, U38.32
- new net SCL38: IN38.13, OUT38.13, U39.32
- new net SCL39: IN39.13, OUT39.13, U40.32
- new net SCL40: IN40.13, OUT40.13, U41.32
- new net SCL41: IN41.13, OUT41.13, U42.32
- new net SCL42: IN42.13, OUT42.13, U43.32
- new net SCL43: IN43.13, OUT43.13, U44.32
- new net SCL44: IN44.13, OUT44.13, U45.32
- new net SCL45: IN45.13, OUT45.13, U46.32
- new net SCL46: IN46.13, OUT46.13, U47.32
- new net SCL47: IN47.13, OUT47.13, U48.32
- new net SCLK30: IN30.4, OUT30.4
- new net SCLK31: IN31.4, OUT31.4
- new net SCLK32: IN32.4, OUT32.4
- new net SCLK33: IN33.4, OUT33.4
- new net SCLK34: IN34.4, OUT34.4
- new net SCLK35: IN35.4, OUT35.4
- new net SCLK36: IN36.4, OUT36.4
- new net SCLK37: IN37.4, OUT37.4
- new net SCLK38: IN38.4, OUT38.4
- new net SCLK39: IN39.4, OUT39.4
- new net SCLK40: IN40.4, OUT40.4
- new net SCLK41: IN41.4, OUT41.4
- new net SCLK42: IN42.4, OUT42.4
- new net SCLK43: IN43.4, OUT43.4
- new net SCLK44: IN44.4, OUT44.4
- new net SCLK45: IN45.4, OUT45.4
- new net SCLK46: IN46.4, OUT46.4
- new net SCLK47: IN47.4, OUT47.4
- new net SDA30: IN30.12, OUT30.12, U31.2
- new net SDA31: IN31.12, OUT31.12, U32.2
- new net SDA32: IN32.12, OUT32.12, U33.2
- new net SDA33: IN33.12, OUT33.12, U34.2
- new net SDA34: IN34.12, OUT34.12, U35.2
- new net SDA35: IN35.12, OUT35.12, U36.2
- new net SDA36: IN36.12, OUT36.12, U37.2
- new net SDA37: IN37.12, OUT37.12, U38.2
- new net SDA38: IN38.12, OUT38.12, U39.2
- new net SDA39: IN39.12, OUT39.12, U40.2
- new net SDA40: IN40.12, OUT40.12, U41.2
- new net SDA41: IN41.12, OUT41.12, U42.2
- new net SDA42: IN42.12, OUT42.12, U43.2
- new net SDA43: IN43.12, OUT43.12, U44.2
- new net SDA44: IN44.12, OUT44.12, U45.2
- new net SDA45: IN45.12, OUT45.12, U46.2
- new net SDA46: IN46.12, OUT46.12, U47.2
- new net SDA47: IN47.12, OUT47.12, U48.2
- new net TXD30: TXD30.1, U31.21
- new net TXD31: TXD31.1, U32.21
- new net TXD32: TXD32.1, U33.21
- new net TXD33: TXD33.1, U34.21
- new net TXD34: TXD34.1, U35.21
- new net TXD35: TXD35.1, U36.21
- new net TXD36: TXD36.1, U37.21
- new net TXD37: TXD37.1, U38.21
- new net TXD38: TXD38.1, U39.21
- new net TXD39: TXD39.1, U40.21
- new net TXD40: TXD40.1, U41.21
- new net TXD41: TXD41.1, U42.21
- new net TXD42: TXD42.1, U43.21
- new net TXD43: TXD43.1, U44.21
- new net TXD44: TXD44.1, U45.21
- new net TXD45: TXD45.1, U46.21
- new net TXD46: TXD46.1, U47.21
- new net TXD47: TXD47.1, U48.21
- new net VDD30: C303.1, C304.1, C309.1, Q31.3, U31.24, U31.25, VDD30.1, V_ANT30.2
- new net VDD31: C313.1, C314.1, C319.1, Q32.3, U32.24, U32.25, VDD31.1, V_ANT31.2
- new net VDD32: C323.1, C324.1, C329.1, Q33.3, U33.24, U33.25, VDD32.1, V_ANT32.2
- new net VDD33: C333.1, C334.1, C339.1, Q34.3, U34.24, U34.25, VDD33.1, V_ANT33.2
- new net VDD34: C343.1, C344.1, C349.1, Q35.3, U35.24, U35.25, VDD34.1, V_ANT34.2
- new net VDD35: C353.1, C354.1, C359.1, Q36.3, U36.24, U36.25, VDD35.1, V_ANT35.2
- new net VDD36: C363.1, C364.1, C369.1, Q37.3, U37.24, U37.25, VDD36.1, V_ANT36.2
- new net VDD37: C373.1, C374.1, C379.1, Q38.3, U38.24, U38.25, VDD37.1, V_ANT37.2
- new net VDD38: C383.1, C384.1, C389.1, Q39.3, U39.24, U39.25, VDD38.1, V_ANT38.2
- new net VDD39: C393.1, C394.1, C399.1, Q40.3, U40.24, U40.25, VDD39.1, V_ANT39.2
- new net VDD40: C403.1, C404.1, C409.1, Q41.3, U41.24, U41.25, VDD40.1, V_ANT40.2
- new net VDD41: C413.1, C414.1, C419.1, Q42.3, U42.24, U42.25, VDD41.1, V_ANT41.2
- new net VDD42: C423.1, C424.1, C429.1, Q43.3, U43.24, U43.25, VDD42.1, V_ANT42.2
- new net VDD43: C433.1, C434.1, C439.1, Q44.3, U44.24, U44.25, VDD43.1, V_ANT43.2
- new net VDD44: C443.1, C444.1, C449.1, Q45.3, U45.24, U45.25, VDD44.1, V_ANT44.2
- new net VDD45: C453.1, C454.1, C459.1, Q46.3, U46.24, U46.25, VDD45.1, V_ANT45.2
- new net VDD46: C463.1, C464.1, C469.1, Q47.3, U47.24, U47.25, VDD46.1, V_ANT46.2
- new net VDD47: C473.1, C474.1, C479.1, Q48.3, U48.24, U48.25, VDD47.1, V_ANT47.2
- new net V_BCKP30: B31.+, C310.1, R93.1, U31.16, V_BCKP30.1
- new net V_BCKP31: B32.+, C320.1, R96.1, U32.16, V_BCKP31.1
- new net V_BCKP32: B33.+, C330.1, R99.1, U33.16, V_BCKP32.1
- new net V_BCKP33: B34.+, C340.1, R102.1, U34.16, V_BCKP33.1
- new net V_BCKP34: B35.+, C350.1, R105.1, U35.16, V_BCKP34.1
- new net V_BCKP35: B36.+, C360.1, R108.1, U36.16, V_BCKP35.1
- new net V_BCKP36: B37.+, C370.1, R111.1, U37.16, V_BCKP36.1
- new net V_BCKP37: B38.+, C380.1, R114.1, U38.16, V_BCKP37.1
- new net V_BCKP38: B39.+, C390.1, R117.1, U39.16, V_BCKP38.1
- new net V_BCKP39: B40.+, C400.1, R120.1, U40.16, V_BCKP39.1
- new net V_BCKP40: B41.+, C410.1, R123.1, U41.16, V_BCKP40.1
- new net V_BCKP41: B42.+, C420.1, R126.1, U42.16, V_BCKP41.1
- new net V_BCKP42: B43.+, C430.1, R129.1, U43.16, V_BCKP42.1
- new net V_BCKP43: B44.+, C440.1, R132.1, U44.16, V_BCKP43.1
- new net V_BCKP44: B45.+, C450.1, R135.1, U45.16, V_BCKP44.1
- new net V_BCKP45: B46.+, C460.1, R138.1, U46.16, V_BCKP45.1
- new net V_BCKP46: B47.+, C470.1, R141.1, U47.16, V_BCKP46.1
- new net V_BCKP47: B48.+, C480.1, R144.1, U48.16, V_BCKP47.1
- new net V_USB30: IN30.16, OUT30.16
- new net V_USB31: IN31.16, OUT31.16
- new net V_USB32: IN32.16, OUT32.16
- new net V_USB33: IN33.16, OUT33.16
- new net V_USB34: IN34.16, OUT34.16
- new net V_USB35: IN35.16, OUT35.16
- new net V_USB36: IN36.16, OUT36.16
- new net V_USB37: IN37.16, OUT37.16
- new net V_USB38: IN38.16, OUT38.16
- new net V_USB39: IN39.16, OUT39.16
- new net V_USB40: IN40.16, OUT40.16
- new net V_USB41: IN41.16, OUT41.16
- new net V_USB42: IN42.16, OUT42.16
- new net V_USB43: IN43.16, OUT43.16
- new net V_USB44: IN44.16, OUT44.16
- new net V_USB45: IN45.16, OUT45.16
- new net V_USB46: IN46.16, OUT46.16
- new net V_USB47: IN47.16, OUT47.16
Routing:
- net 3.3V30: track 0.00 -> 126.5 mm, vias 0 -> 8
- net 3.3V46: track 0.00 -> 126.5 mm, vias 0 -> 8
- net 3.3V42: track 0.00 -> 126.5 mm, vias 0 -> 8
- net 3.3V31: track 0.00 -> 126.5 mm, vias 0 -> 8
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- added copper zone on layer 1, net GND30
- added copper zone on layer 15, net GND30
- added copper zone on layer 16, net GND30
- added copper zone on layer 2, net GND30
- added copper zone on layer 1, net GND31
- added copper zone on layer 15, net GND31
- added copper zone on layer 16, net GND31
- added copper zone on layer 2, net GND31
- added copper zone on layer 1, net GND32
- added copper zone on layer 15, net GND32
- added copper zone on layer 16, net GND32
- added copper zone on layer 2, net GND32
- added copper zone on layer 1, net GND33
- added copper zone on layer 15, net GND33
- added copper zone on layer 16, net GND33
- added copper zone on layer 2, net GND33
- added copper zone on layer 1, net GND34
- added copper zone on layer 15, net GND34
- added copper zone on layer 16, net GND34
- added copper zone on layer 2, net GND34
- added copper zone on layer 1, net GND35
- added copper zone on layer 15, net GND35
- added copper zone on layer 16, net GND35
- added copper zone on layer 2, net GND35
- added copper zone on layer 1, net GND36
- added copper zone on layer 15, net GND36
- added copper zone on layer 16, net GND36
- added copper zone on layer 2, net GND36
- added copper zone on layer 1, net GND37
- added copper zone on layer 15, net GND37
- added copper zone on layer 16, net GND37
- added copper zone on layer 2, net GND37
- added copper zone on layer 1, net GND38
- added copper zone on layer 15, net GND38
- added copper zone on layer 16, net GND38
- added copper zone on layer 2, net GND38
- added copper zone on layer 1, net GND39
- added copper zone on layer 15, net GND39
- added copper zone on layer 16, net GND39
- added copper zone on layer 2, net GND39
- added copper zone on layer 1, net GND40
- added copper zone on layer 15, net GND40
- added copper zone on layer 16, net GND40
- added copper zone on layer 2, net GND40
- added copper zone on layer 1, net GND41
- added copper zone on layer 15, net GND41
- added copper zone on layer 16, net GND41
- added copper zone on layer 2, net GND41
- added copper zone on layer 1, net GND42
- added copper zone on layer 15, net GND42
- added copper zone on layer 16, net GND42
- added copper zone on layer 2, net GND42
- added copper zone on layer 1, net GND43
- added copper zone on layer 15, net GND43
- added copper zone on layer 16, net GND43
- added copper zone on layer 2, net GND43
- added copper zone on layer 1, net GND44
- added copper zone on layer 15, net GND44
- added copper zone on layer 16, net GND44
- added copper zone on layer 2, net GND44
- added copper zone on layer 1, net GND45
- added copper zone on layer 15, net GND45
- added copper zone on layer 16, net GND45
- added copper zone on layer 2, net GND45
- added copper zone on layer 1, net GND46
- added copper zone on layer 15, net GND46
- added copper zone on layer 16, net GND46
- added copper zone on layer 2, net GND46
- added copper zone on layer 1, net GND47
- added copper zone on layer 15, net GND47
- added copper zone on layer 16, net GND47
- added copper zone on layer 2, net GND47
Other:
- board size 187.2 x 136.7 mm -> 198.4 x 137.2 mm
- board text removed: "Route Out"

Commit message: Change R2 to RES-15724
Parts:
- IN, IN1, IN10, IN11, IN12, IN13, IN14, IN15, IN16, IN17, IN18, IN19, IN2, IN20, IN21, IN22, IN23, IN24, IN25, IN26, IN27, IN28, IN29, IN3, IN30, IN31, IN32, IN33, IN34, IN35, IN36, IN37, IN38, IN39, IN4, IN40, IN41, IN42, IN43, IN44, IN45, IN46, IN47, IN5, IN6, IN7, IN8, IN9, OUT, OUT1, OUT10, OUT11, OUT12, OUT13, OUT14, OUT15, OUT16, OUT17, OUT18, OUT19, OUT2, OUT20, OUT21, OUT22, OUT23, OUT24, OUT25, OUT26, OUT27, OUT28, OUT29, OUT3, OUT30, OUT31, OUT32, OUT33, OUT34, OUT35, OUT36, OUT37, OUT38, OUT39, OUT4, OUT40, OUT41, OUT42, OUT43, OUT44, OUT45, OUT46, OUT47, OUT5, OUT6, OUT7, OUT8, OUT9: value FPC_16_0.5MM_BACKFLIP -> (none); device New_Parts_Connectors:FPC_16_DOUBLESIDED_BACKFLIP -> SparkFun-Connectors:FPC_16_0.5MM
